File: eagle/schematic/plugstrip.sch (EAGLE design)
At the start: 30 parts, among them U1 Hall Effect, U2 Current ADC, U3 Voltage ADC

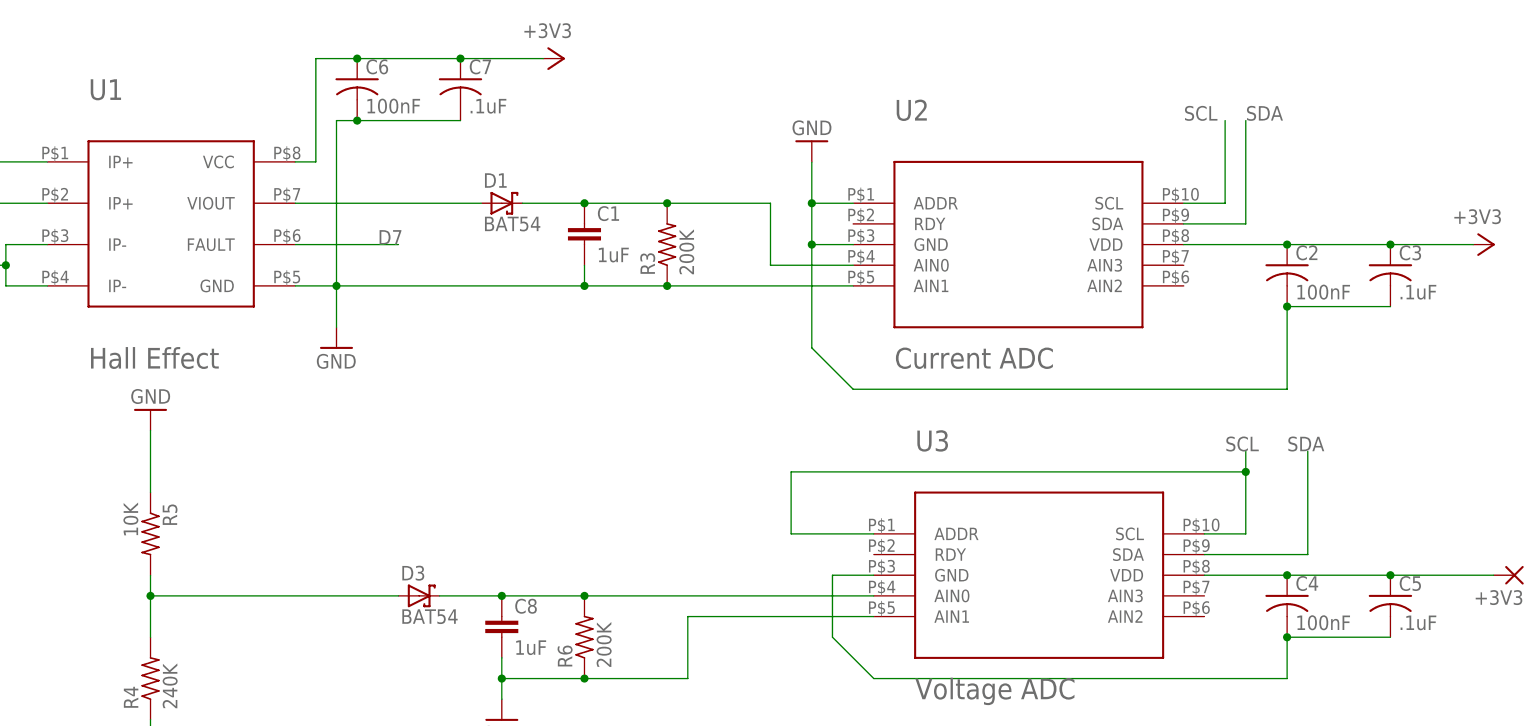
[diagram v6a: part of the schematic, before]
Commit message: update schematic
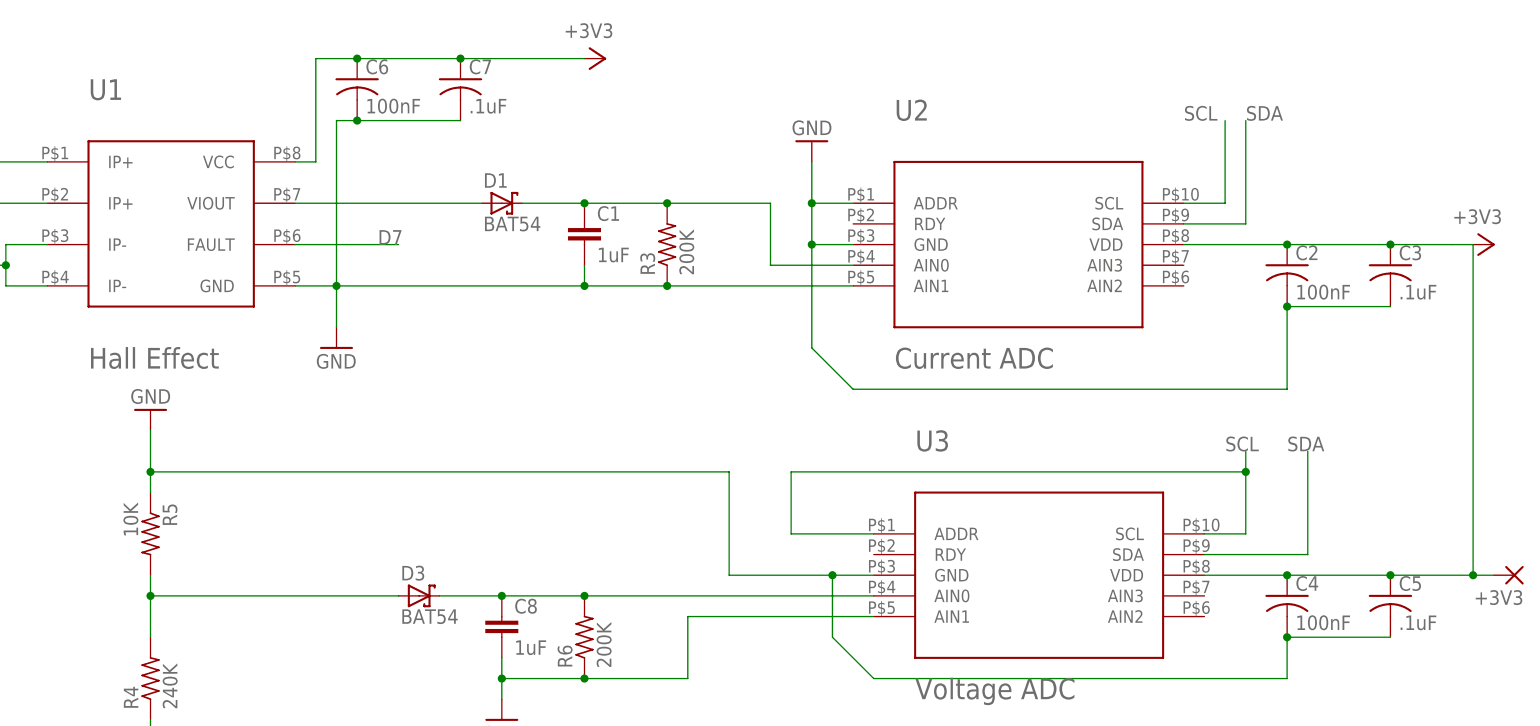
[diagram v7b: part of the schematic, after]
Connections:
- removed net N$14: C4.2, C5.2, U3.GND
- removed net N$3: +3V3.P, C4.1, C5.1, U3.VDD
- net +3V3: now also +3V3.P, C4.1, C5.1, U3.VDD
- net GND: now also C4.2, C5.2, U3.GND
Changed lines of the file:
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@@
 <instance part="GND2" gate="1" x="-81.28" y="-81.28"/>
 <instance part="GND3" gate="1" x="17.78" y="20.32"/>
-<instance part="+3V1" gate="G$1" x="45.72" y="55.88" rot="R270"/>
+<instance part="+3V1" gate="G$1" x="50.8" y="55.88" rot="R270"/>
 <instance part="D1" gate="G$1" x="38.1" y="38.1"/>
 <instance part="C1" gate="G$1" x="48.26" y="35.56"/>
@@
 <pinref part="GND17" gate="1" pin="GND"/>
 <pinref part="R5" gate="G$1" pin="1"/>
-<wire x1="-5.08" y1="2.54" x2="-5.08" y2="10.16" width="0.1524" layer="91"/>
+<wire x1="-5.08" y1="2.54" x2="-5.08" y2="5.08" width="0.1524" layer="91"/>
+<wire x1="-5.08" y1="5.08" x2="-5.08" y2="10.16" width="0.1524" layer="91"/>
+<wire x1="-5.08" y1="5.08" x2="66.04" y2="5.08" width="0.1524" layer="91"/>
+<wire x1="66.04" y1="5.08" x2="66.04" y2="-7.62" width="0.1524" layer="91"/>
+<junction x="-5.08" y="5.08"/>
+<pinref part="U3" gate="G$1" pin="GND"/>
+<wire x1="83.82" y1="-7.62" x2="78.74" y2="-7.62" width="0.1524" layer="91"/>
+<pinref part="C5" gate="G$1" pin="2"/>
+<pinref part="C4" gate="G$1" pin="2"/>
+<wire x1="147.32" y1="-15.24" x2="134.62" y2="-15.24" width="0.1524" layer="91"/>
+<wire x1="134.62" y1="-15.24" x2="134.62" y2="-20.32" width="0.1524" layer="91"/>
+<junction x="134.62" y="-15.24"/>
+<wire x1="134.62" y1="-20.32" x2="83.82" y2="-20.32" width="0.1524" layer="91"/>
+<wire x1="83.82" y1="-20.32" x2="78.74" y2="-15.24" width="0.1524" layer="91"/>
+<wire x1="78.74" y1="-15.24" x2="78.74" y2="-7.62" width="0.1524" layer="91"/>
+<wire x1="66.04" y1="-7.62" x2="78.74" y2="-7.62" width="0.1524" layer="91"/>
+<junction x="78.74" y="-7.62"/>
 </segment>
 <segment>
@@
 <junction x="134.62" y="33.02"/>
 <pinref part="+3V2" gate="G$1" pin="+3V3"/>
-<wire x1="147.32" y1="33.02" x2="157.48" y2="33.02" width="0.1524" layer="91"/>
+<wire x1="147.32" y1="33.02" x2="154.94" y2="33.02" width="0.1524" layer="91"/>
 <junction x="147.32" y="33.02"/>
+<pinref part="U3" gate="G$1" pin="VDD"/>
+<pinref part="C4" gate="G$1" pin="1"/>
+<wire x1="124.46" y1="-7.62" x2="134.62" y2="-7.62" width="0.1524" layer="91"/>
+<pinref part="C5" gate="G$1" pin="1"/>
+<wire x1="134.62" y1="-7.62" x2="147.32" y2="-7.62" width="0.1524" layer="91"/>
+<junction x="134.62" y="-7.62"/>
+<pinref part="+3V3" gate="1" pin="P"/>
+<wire x1="147.32" y1="-7.62" x2="157.48" y2="-7.62" width="0.1524" layer="91"/>
+<junction x="147.32" y="-7.62"/>
+<wire x1="157.48" y1="-7.62" x2="160.02" y2="-7.62" width="0.1524" layer="91"/>
+<wire x1="154.94" y1="33.02" x2="157.48" y2="33.02" width="0.1524" layer="91"/>
+<wire x1="157.48" y1="33.02" x2="157.48" y2="-7.62" width="0.1524" layer="91"/>
+<junction x="157.48" y="-7.62"/>
 </segment>
 <segment>
@@
 <junction x="20.32" y="55.88"/>
 <pinref part="+3V1" gate="G$1" pin="+3V3"/>
-<wire x1="33.02" y1="55.88" x2="43.18" y2="55.88" width="0.1524" layer="91"/>
+<wire x1="33.02" y1="55.88" x2="48.26" y2="55.88" width="0.1524" layer="91"/>
 <junction x="33.02" y="55.88"/>
 </segment>
@@
 </segment>
 </net>
-<net name="N$3" class="0">
-<segment>
-<pinref part="U3" gate="G$1" pin="VDD"/>
-<pinref part="C4" gate="G$1" pin="1"/>
-<wire x1="124.46" y1="-7.62" x2="134.62" y2="-7.62" width="0.1524" layer="91"/>
-<pinref part="C5" gate="G$1" pin="1"/>
-<wire x1="134.62" y1="-7.62" x2="147.32" y2="-7.62" width="0.1524" layer="91"/>
-<junction x="134.62" y="-7.62"/>
-<pinref part="+3V3" gate="1" pin="P"/>
-<wire x1="147.32" y1="-7.62" x2="160.02" y2="-7.62" width="0.1524" layer="91"/>
-<junction x="147.32" y="-7.62"/>
-</segment>
-</net>
 <net name="N$4" class="0">
 <segment>
@@
 </segment>
 </net>
-<net name="N$14" class="0">
-<segment>
-<pinref part="U3" gate="G$1" pin="GND"/>
-<wire x1="83.82" y1="-7.62" x2="78.74" y2="-7.62" width="0.1524" layer="91"/>
-<pinref part="C5" gate="G$1" pin="2"/>
-<pinref part="C4" gate="G$1" pin="2"/>
-<wire x1="147.32" y1="-15.24" x2="134.62" y2="-15.24" width="0.1524" layer="91"/>
-<wire x1="134.62" y1="-15.24" x2="134.62" y2="-20.32" width="0.1524" layer="91"/>
-<junction x="134.62" y="-15.24"/>
-<wire x1="134.62" y1="-20.32" x2="83.82" y2="-20.32" width="0.1524" layer="91"/>
-<wire x1="83.82" y1="-20.32" x2="78.74" y2="-15.24" width="0.1524" layer="91"/>
-<wire x1="78.74" y1="-15.24" x2="78.74" y2="-7.62" width="0.1524" layer="91"/>
-</segment>
-</net>

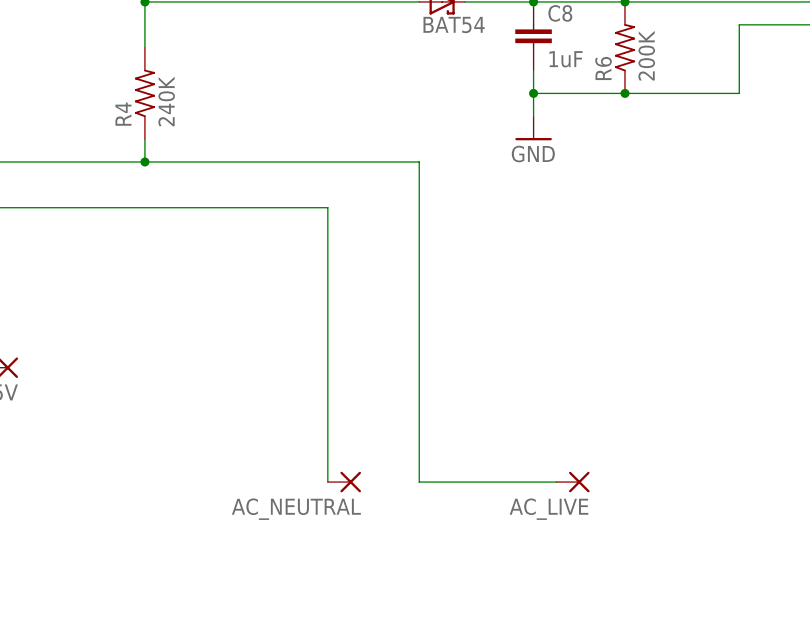
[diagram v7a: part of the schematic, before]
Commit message: add fuse, remove ground routing
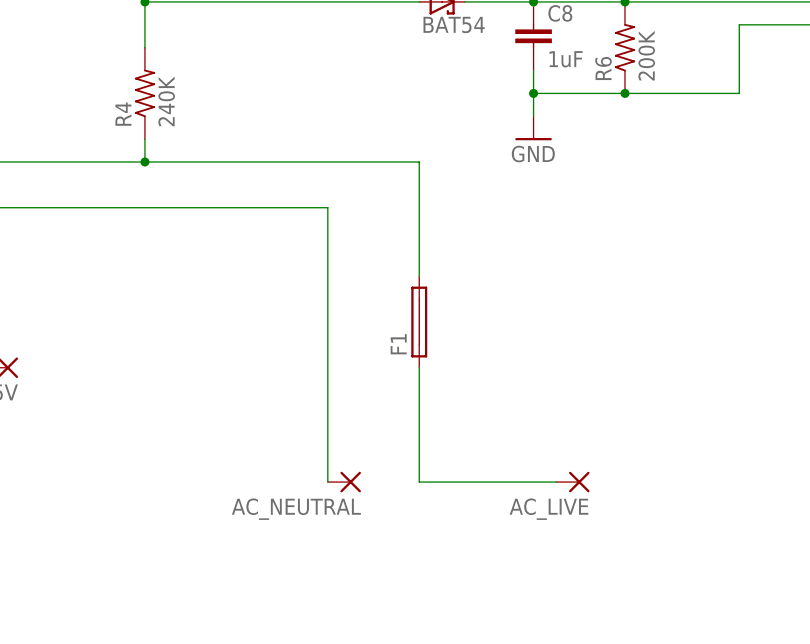
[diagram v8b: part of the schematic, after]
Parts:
- added F1: (no value), fuse:19560
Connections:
- new net N$14: AC_LIVE.P, F1.1
- net AC_LIVE: now also F1.2; no longer AC_LIVE.P
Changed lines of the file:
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@@
 <part name="R6" library="jackIdd" deviceset="R-US_" device="CT14J" value="200K"/>
 <part name="GND5" library="supply1" deviceset="GND" device=""/>
+<part name="F1" library="fuse" deviceset="19560" device=""/>
 </parts>
 <sheets>
@@
 <instance part="R6" gate="G$1" x="48.26" y="-15.24" rot="R90"/>
 <instance part="GND5" gate="1" x="38.1" y="-25.4"/>
+<instance part="F1" gate="F" x="25.4" y="-45.72" rot="R90"/>
 </instances>
 <busses>
@@
 <pinref part="R4" gate="G$1" pin="1"/>
 <wire x1="-5.08" y1="-25.4" x2="-5.08" y2="-27.94" width="0.1524" layer="91"/>
-<pinref part="AC_LIVE" gate="1" pin="P"/>
-<wire x1="40.64" y1="-63.5" x2="25.4" y2="-63.5" width="0.1524" layer="91"/>
-<wire x1="25.4" y1="-63.5" x2="25.4" y2="-27.94" width="0.1524" layer="91"/>
 <wire x1="25.4" y1="-27.94" x2="-5.08" y2="-27.94" width="0.1524" layer="91"/>
 <junction x="-5.08" y="-27.94"/>
+<pinref part="F1" gate="F" pin="2"/>
+<wire x1="25.4" y1="-27.94" x2="25.4" y2="-40.64" width="0.1524" layer="91"/>
 </segment>
 </net>
@@
 </segment>
 </net>
+<net name="N$14" class="1">
+<segment>
+<pinref part="AC_LIVE" gate="1" pin="P"/>
+<wire x1="40.64" y1="-63.5" x2="25.4" y2="-63.5" width="0.1524" layer="91"/>
+<pinref part="F1" gate="F" pin="1"/>
+<wire x1="25.4" y1="-50.8" x2="25.4" y2="-63.5" width="0.1524" layer="91"/>
+</segment>
+</net>
